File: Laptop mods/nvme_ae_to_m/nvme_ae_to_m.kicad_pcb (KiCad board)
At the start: 2 copper layers, 22 x 26 mm, 23 parts, among them J1 USB, U1 NGFF_M, U2 NGFF_AE

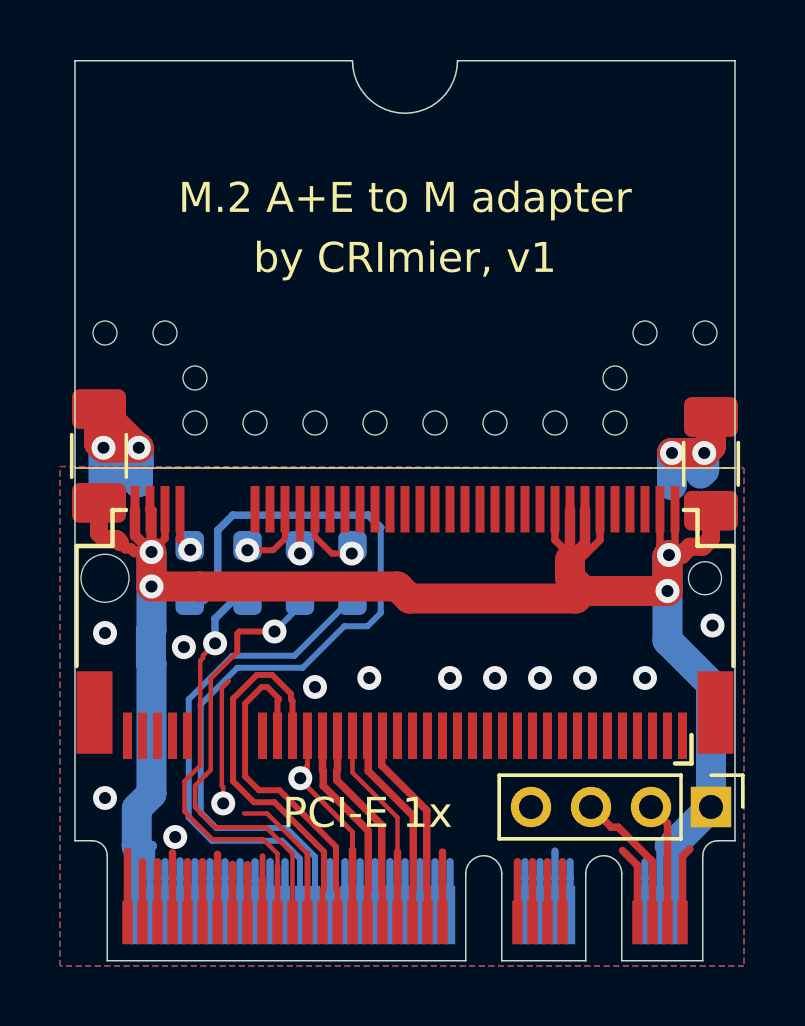
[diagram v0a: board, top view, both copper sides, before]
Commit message: nvme_ae_to_m: v2, fixed tx/rx pair swaps, removed caps
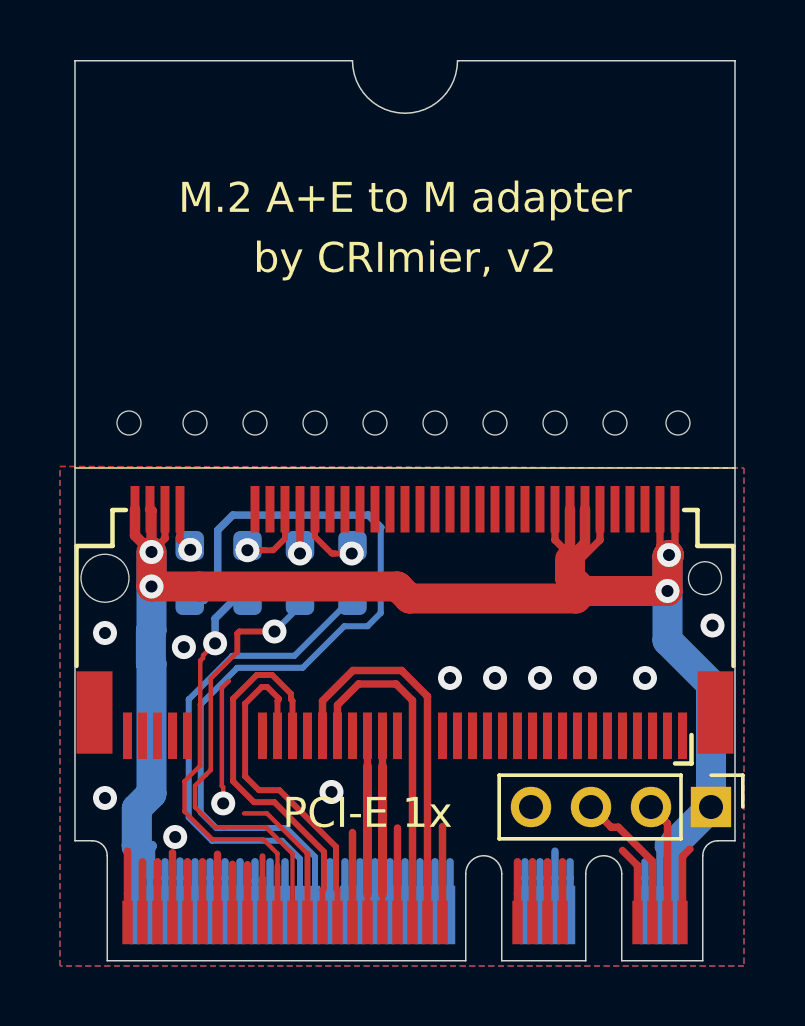
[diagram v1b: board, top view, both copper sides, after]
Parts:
- removed C1, C2: 10uF, Capacitor_SMD:C_1206_3216Metric_Pad1.33x1.80mm_HandSolder
- removed the REF** at (133.0, 151.5)
- removed the REF** at (130.0, 150.0)
- removed the REF** at (150.0, 150.0)
- removed the REF** at (147.0, 151.5)
- moved REF** 3.23 mm to (130.8, 153.0)
- moved REF** 3.20 mm to (149.1, 153.0)
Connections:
- net /PCIE_~SATA renamed /PCIE_~{SATA}
- net ~CLKREQ renamed ~{CLKREQ}
- net ~PERST renamed ~{PERST}
- net ~PEWAKE renamed ~{PEWAKE}
- U1 pad 41: /PER0- -> /PET0+
- U1 pad 43: /PER0+ -> /PET0-
- U1 pad 47: /PET0- -> /PER0-
- U1 pad 49: /PET0+ -> /PER0+
- U1 pad 53: /REFCLK+ -> /REFCLK-
- U1 pad 55: /REFCLK- -> /REFCLK+
- U2 pad 35: /PER0- -> /PER0+
- U2 pad 37: /PER0+ -> /PER0-
- U2 pad 41: /PET0- -> /PET0+
- U2 pad 43: /PET0+ -> /PET0-
- U2 pad 47: /REFCLK- -> /REFCLK+
- U2 pad 49: /REFCLK+ -> /REFCLK-
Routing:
- net GND: track 66.3 -> 36.5 mm, vias 18 -> 12
- net /PER0+: track 6.87 -> 13.9 mm
- net +3V3: track 74.7 -> 69.2 mm
- net /PER0-: track 6.87 -> 11.4 mm
- net /REFCLK-: track 11.7 -> 13.1 mm
- net /REFCLK+: track 13.1 -> 11.7 mm
- net /PET0-: track 6.87 -> 6.22 mm
- net /PET0+: track 6.87 -> 6.22 mm
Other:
- net class Default removed
- board text added: "by CRImier, v2"
- board text added: "trans rights"
- board text removed: "by CRImier, v1"
